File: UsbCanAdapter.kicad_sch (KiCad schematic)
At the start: 32 parts, among them J1 Screw_Terminal_01x04, J2 USB_C_Receptacle_USB2.0, J3 SWD Pads, SW1 SW_Push, U1 STM32F042C6Tx, U3 MCP1700x-330xxTT

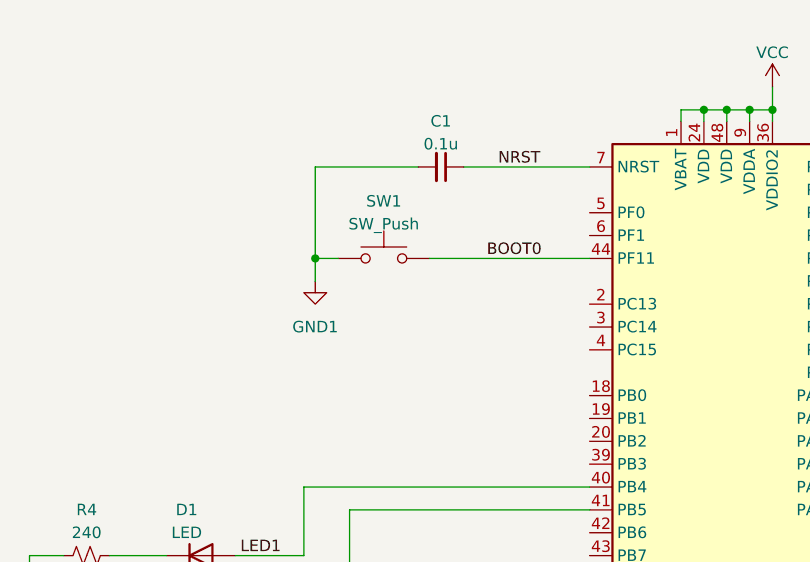
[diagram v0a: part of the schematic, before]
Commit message: Fix rev1 issues
- reverse BOOT0 pin polarity
- enlarge short jumper holes to 1mm
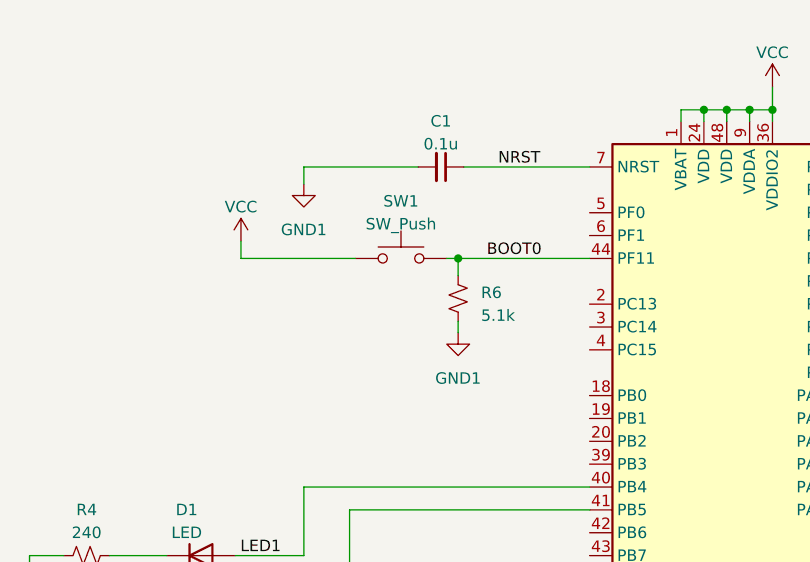
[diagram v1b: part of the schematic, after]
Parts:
- added R6: 5.1k, Resistor_SMD:R_0603_1608Metric, symbol Device:R_Small_US
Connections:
- net BOOT0: now also R6.1
- net GND1: now also R6.2; no longer SW1.1
- net VCC: now also SW1.1
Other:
- moved on the sheet: SW1
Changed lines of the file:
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@@
   (junction (at 127 25.4) (diameter 0) (color 0 0 0 0)
   )
+  (junction (at 69.215 46.99) (diameter 0) (color 0 0 0 0)
+  )
   (junction (at 156.21 86.36) (diameter 0) (color 0 0 0 0)
   )
@@
   (junction (at 77.47 160.02) (diameter 0) (color 0 0 0 0)
   )
-  (junction (at 53.34 46.99) (diameter 0) (color 0 0 0 0)
-  )
   (junction (at 149.86 33.02) (diameter 0) (color 0 0 0 0)
   )
@@
     (stroke (width 0) (type default))
   )
-  (wire (pts (xy 55.88 46.99) (xy 53.34 46.99))
+  (wire (pts (xy 45.085 46.99) (xy 57.785 46.99))
     (stroke (width 0) (type default))
   )
@@
     (stroke (width 0) (type default))
   )
+  (wire (pts (xy 69.215 53.975) (xy 69.215 55.245))
+    (stroke (width 0) (type default))
+  )
   (wire (pts (xy 144.78 73.66) (xy 157.48 73.66))
     (stroke (width 0) (type default))
@@
     (stroke (width 0) (type default))
   )
-  (wire (pts (xy 53.34 46.99) (xy 53.34 49.53))
-    (stroke (width 0) (type default))
-  )
   (wire (pts (xy 93.98 109.22) (xy 99.06 109.22))
     (stroke (width 0) (type default))
@@
     (stroke (width 0) (type default))
   )
-  (wire (pts (xy 64.77 36.83) (xy 53.34 36.83))
+  (wire (pts (xy 52.07 36.83) (xy 64.77 36.83))
     (stroke (width 0) (type default))
   )
@@
     (stroke (width 0) (type default))
   )
+  (wire (pts (xy 69.215 46.99) (xy 69.215 48.895))
+    (stroke (width 0) (type default))
+  )
   (wire (pts (xy 33.02 182.88) (xy 36.83 182.88))
     (stroke (width 0) (type default))
@@
     (stroke (width 0) (type default))
   )
+  (wire (pts (xy 45.085 45.085) (xy 45.085 46.99))
+    (stroke (width 0) (type default))
+  )
   (wire (pts (xy 100.33 151.13) (xy 100.33 152.4))
     (stroke (width 0) (type default))
@@
     (stroke (width 0) (type default))
   )
-  (wire (pts (xy 53.34 36.83) (xy 53.34 46.99))
-    (stroke (width 0) (type default))
-  )
   (wire (pts (xy 57.15 153.67) (xy 57.15 156.21))
     (stroke (width 0) (type default))
@@
     (stroke (width 0) (type default))
   )
+  (wire (pts (xy 52.07 38.735) (xy 52.07 36.83))
+    (stroke (width 0) (type default))
+  )
   (wire (pts (xy 114.3 140.97) (xy 114.3 137.16))
     (stroke (width 0) (type default))
@@
     (stroke (width 0) (type default))
   )
-  (wire (pts (xy 66.04 46.99) (xy 83.82 46.99))
+  (wire (pts (xy 67.945 46.99) (xy 69.215 46.99))
+    (stroke (width 0) (type default))
+  )
+  (wire (pts (xy 69.215 46.99) (xy 83.82 46.99))
     (stroke (width 0) (type default))
   )
@@
     )
   )
-  (symbol (lib_id "power:GND1") (at 53.34 49.53 0) (unit 1)
-    (in_bom yes) (on_board yes) (dnp no) (fields_autoplaced)
-    (property "Reference" "#PWR012" (at 53.34 55.88 0)
-      (effects (font (size 1.27 1.27)) hide)
-    )
-    (property "Value" "GND1" (at 53.34 54.61 0)
-      (effects (font (size 1.27 1.27)))
-    )
-    (property "Footprint" "" (at 53.34 49.53 0)
-      (effects (font (size 1.27 1.27)) hide)
-    )
-    (property "Datasheet" "" (at 53.34 49.53 0)
+  (symbol (lib_id "power:GND1") (at 52.07 38.735 0) (unit 1)
+    (in_bom yes) (on_board yes) (dnp no) (fields_autoplaced)
+    (property "Reference" "#PWR012" (at 52.07 45.085 0)
+      (effects (font (size 1.27 1.27)) hide)
+    )
+    (property "Value" "GND1" (at 52.07 43.815 0)
+      (effects (font (size 1.27 1.27)))
+    )
+    (property "Footprint" "" (at 52.07 38.735 0)
+      (effects (font (size 1.27 1.27)) hide)
+    )
+    (property "Datasheet" "" (at 52.07 38.735 0)
       (effects (font (size 1.27 1.27)) hide)
     )
@@
     )
   )
-  (symbol (lib_id "Switch:SW_Push") (at 60.96 46.99 0) (unit 1)
-    (in_bom yes) (on_board yes) (dnp no) (fields_autoplaced)
-    (property "Reference" "SW1" (at 60.96 40.64 0)
-      (effects (font (size 1.27 1.27)))
-    )
-    (property "Value" "SW_Push" (at 60.96 43.18 0)
-      (effects (font (size 1.27 1.27)))
-    )
-    (property "Footprint" "Button_Switch_SMD:SW_SPST_PTS810" (at 60.96 41.91 0)
-      (effects (font (size 1.27 1.27)) hide)
-    )
-    (property "Datasheet" "~" (at 60.96 41.91 0)
-      (effects (font (size 1.27 1.27)) hide)
-    )
-    (property "Mfg Part Number" "PTS810 SJM 250 SMTR LFS" (at 60.96 46.99 0)
-      (effects (font (size 1.27 1.27)) hide)
-    )
-    (property "DK Part Number" "CKN10502CT-ND" (at 60.96 46.99 0)
+  (symbol (lib_id "Switch:SW_Push") (at 62.865 46.99 0) (unit 1)
+    (in_bom yes) (on_board yes) (dnp no) (fields_autoplaced)
+    (property "Reference" "SW1" (at 62.865 40.64 0)
+      (effects (font (size 1.27 1.27)))
+    )
+    (property "Value" "SW_Push" (at 62.865 43.18 0)
+      (effects (font (size 1.27 1.27)))
+    )
+    (property "Footprint" "Button_Switch_SMD:SW_SPST_PTS810" (at 62.865 41.91 0)
+      (effects (font (size 1.27 1.27)) hide)
+    )
+    (property "Datasheet" "~" (at 62.865 41.91 0)
+      (effects (font (size 1.27 1.27)) hide)
+    )
+    (property "Mfg Part Number" "PTS810 SJM 250 SMTR LFS" (at 62.865 46.99 0)
+      (effects (font (size 1.27 1.27)) hide)
+    )
+    (property "DK Part Number" "CKN10502CT-ND" (at 62.865 46.99 0)
       (effects (font (size 1.27 1.27)) hide)
     )
@@
     )
   )
+  (symbol (lib_id "power:VCC") (at 45.085 45.085 0) (unit 1)
+    (in_bom yes) (on_board yes) (dnp no)
+    (property "Reference" "#PWR024" (at 45.085 48.895 0)
+      (effects (font (size 1.27 1.27)) hide)
+    )
+    (property "Value" "VCC" (at 45.085 41.275 0)
+      (effects (font (size 1.27 1.27)))
+    )
+    (property "Footprint" "" (at 45.085 45.085 0)
+      (effects (font (size 1.27 1.27)) hide)
+    )
+    (property "Datasheet" "" (at 45.085 45.085 0)
+      (effects (font (size 1.27 1.27)) hide)
+    )
+    (pin "1")
+    (instances
+      (project "UsbCanAdapter"
+        (path "/b43f43ba-a9f1-45fb-9930-c904e256e54e"
+          (reference "#PWR024") (unit 1)
+        )
+      )
+    )
+  )
   (symbol (lib_id "Device:LED") (at 40.64 88.9 0) (unit 1)
     (in_bom yes) (on_board yes) (dnp no) (fields_autoplaced)
@@
     )
   )
+  (symbol (lib_id "power:GND1") (at 69.215 55.245 0) (unit 1)
+    (in_bom yes) (on_board yes) (dnp no) (fields_autoplaced)
+    (property "Reference" "#PWR025" (at 69.215 61.595 0)
+      (effects (font (size 1.27 1.27)) hide)
+    )
+    (property "Value" "GND1" (at 69.215 60.325 0)
+      (effects (font (size 1.27 1.27)))
+    )
+    (property "Footprint" "" (at 69.215 55.245 0)
+      (effects (font (size 1.27 1.27)) hide)
+    )
+    (property "Datasheet" "" (at 69.215 55.245 0)
+      (effects (font (size 1.27 1.27)) hide)
+    )
+    (pin "1")
+    (instances
+      (project "UsbCanAdapter"
+        (path "/b43f43ba-a9f1-45fb-9930-c904e256e54e"
+          (reference "#PWR025") (unit 1)
+        )
+      )
+    )
+  )
   (symbol (lib_id "power:VCC") (at 158.75 109.22 0) (unit 1)
     (in_bom yes) (on_board yes) (dnp no) (fields_autoplaced)
@@
         )
       )
+    )
+  )
+  (symbol (lib_id "Device:R_Small_US") (at 69.215 51.435 0) (unit 1)
+    (in_bom yes) (on_board yes) (dnp no) (fields_autoplaced)
+    (property "Reference" "R6" (at 71.755 50.8 0)
+      (effects (font (size 1.27 1.27)) (justify left))
+    )
+    (property "Value" "5.1k" (at 71.755 53.34 0)
+      (effects (font (size 1.27 1.27)) (justify left))
+    )
+    (property "Footprint" "Resistor_SMD:R_0603_1608Metric" (at 69.215 51.435 0)
+      (effects (font (size 1.27 1.27)) hide)
+    )
+    (property "Datasheet" "~" (at 69.215 51.435 0)
+      (effects (font (size 1.27 1.27)) hide)
+    )
+    (pin "1")
+    (pin "2")
+    (instances
+      (project "UsbCanAdapter"
+        (path "/b43f43ba-a9f1-45fb-9930-c904e256e54e"
+          (reference "R6") (unit 1)
+        )
+      )
